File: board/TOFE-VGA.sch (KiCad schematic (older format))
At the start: 0 parts

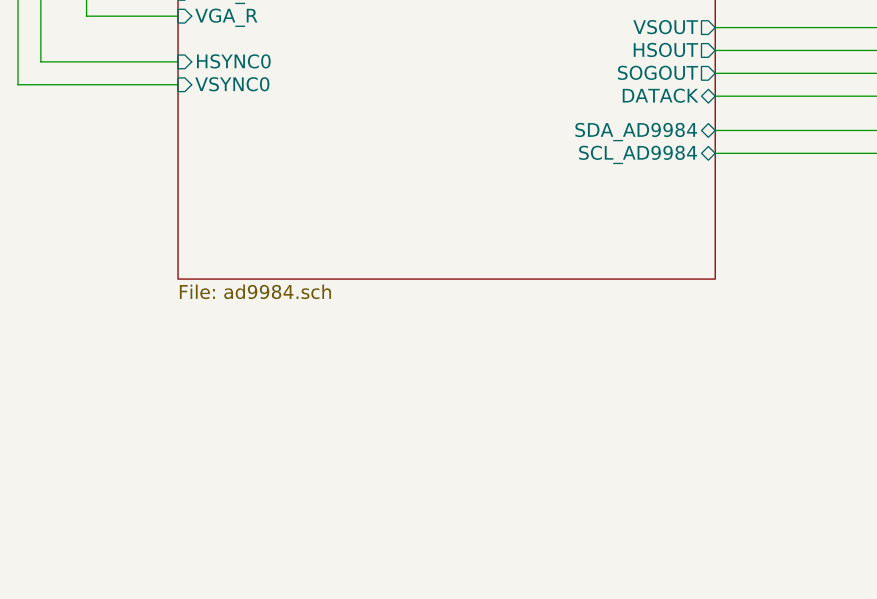
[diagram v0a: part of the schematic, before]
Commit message: Revert "Remove component input to allow design to fit on smaller and much cheaper board"
This reverts commit 3f82e6bce0114ba152d89a6e304191ec714e8d54.
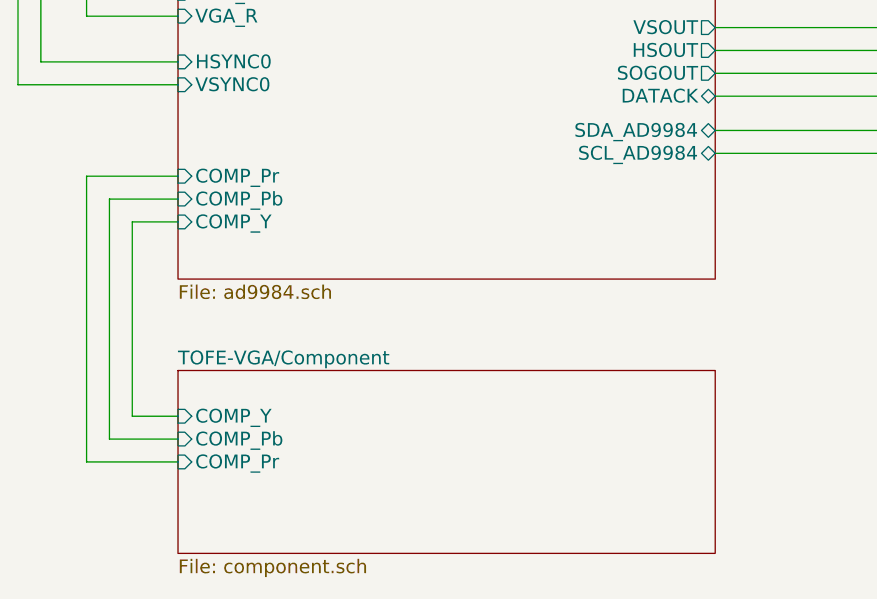
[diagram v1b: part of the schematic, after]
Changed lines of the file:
@@
 $Descr A4 11693 8268
 encoding utf-8
-Sheet 1 5
+Sheet 1 6
 Title "TOFE VGA Expansion Board"
-Date "2016-01-20"
+Date "2016-01-10"
 Rev "1.0"
 Comp "Kenny Duffus <kenny@duffus.org>"
@@
 F14 "SCL_AD9984" B R 5550 4950 60
 F15 "VSOUT" O R 5550 4400 60
+F16 "COMP_Y" I L 3200 5250 60
+F17 "COMP_Pb" I L 3200 5150 60
+F18 "COMP_Pr" I L 3200 5050 60
 $EndSheet
 $Sheet
@@
 Wire Bus Line
 	5550 4200 6550 4200
+$Sheet
+S 3200 5900 2350 800
+U 56559E6B
+F0 "TOFE-VGA/Component" 60
+F1 "component.sch" 60
+F2 "COMP_Y" I L 3200 6100 60
+F3 "COMP_Pb" I L 3200 6200 60
+F4 "COMP_Pr" I L 3200 6300 60
+$EndSheet
 Wire Wire Line
 	3200 4550 2600 4550
@@
 	2600 4550 2600 2450
 Wire Wire Line
+	3200 5250 3000 5250
+Wire Wire Line
+	3000 5250 3000 6100
+Wire Wire Line
+	3000 6100 3200 6100
+Wire Wire Line
+	3200 6200 2900 6200
+Wire Wire Line
+	2900 6200 2900 5150
+Wire Wire Line
+	2900 5150 3200 5150
+Wire Wire Line
+	3200 5050 2800 5050
+Wire Wire Line
+	2800 5050 2800 6300
+Wire Wire Line
+	2800 6300 3200 6300
+Wire Wire Line
 	5550 4700 6550 4700

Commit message: Remove component input to allow design to fit on smaller and much cheaper board
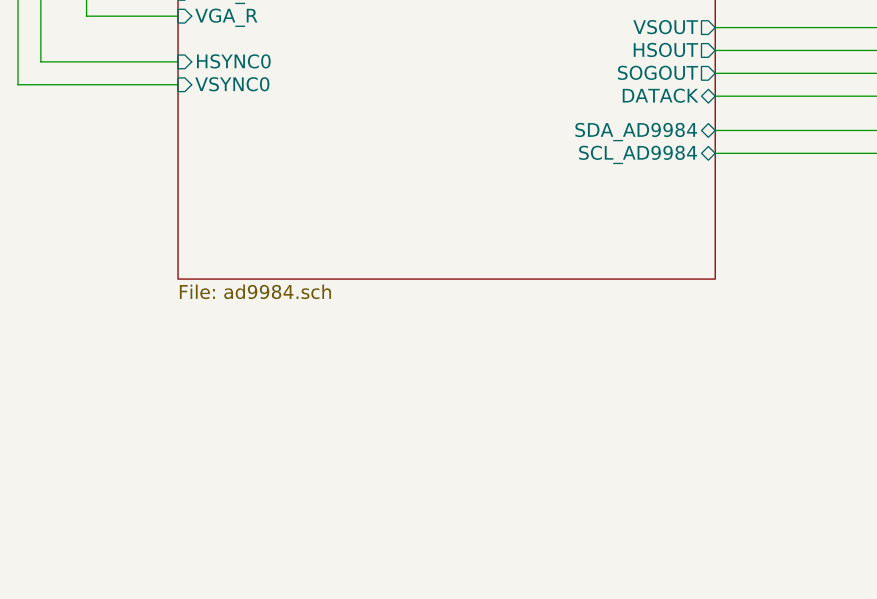
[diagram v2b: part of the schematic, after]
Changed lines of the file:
@@
 $Descr A4 11693 8268
 encoding utf-8
-Sheet 1 6
+Sheet 1 5
 Title "TOFE VGA Expansion Board"
-Date "2016-01-10"
+Date "2016-01-20"
 Rev "1.0"
 Comp "Kenny Duffus <kenny@duffus.org>"
@@
 F14 "SCL_AD9984" B R 5550 4950 60
 F15 "VSOUT" O R 5550 4400 60
-F16 "COMP_Y" I L 3200 5250 60
-F17 "COMP_Pb" I L 3200 5150 60
-F18 "COMP_Pr" I L 3200 5050 60
 $EndSheet
 $Sheet
@@
 Wire Bus Line
 	5550 4200 6550 4200
-$Sheet
-S 3200 5900 2350 800
-U 56559E6B
-F0 "TOFE-VGA/Component" 60
-F1 "component.sch" 60
-F2 "COMP_Y" I L 3200 6100 60
-F3 "COMP_Pb" I L 3200 6200 60
-F4 "COMP_Pr" I L 3200 6300 60
-$EndSheet
 Wire Wire Line
 	3200 4550 2600 4550
@@
 	2600 4550 2600 2450
 Wire Wire Line
-	3200 5250 3000 5250
-Wire Wire Line
-	3000 5250 3000 6100
-Wire Wire Line
-	3000 6100 3200 6100
-Wire Wire Line
-	3200 6200 2900 6200
-Wire Wire Line
-	2900 6200 2900 5150
-Wire Wire Line
-	2900 5150 3200 5150
-Wire Wire Line
-	3200 5050 2800 5050
-Wire Wire Line
-	2800 5050 2800 6300
-Wire Wire Line
-	2800 6300 3200 6300
-Wire Wire Line
 	5550 4700 6550 4700
